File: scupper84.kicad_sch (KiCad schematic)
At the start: 172 parts, among them K1 PG1350, K10 PG1350, K11 PG1350, K12 PG1350, K13 PG1350, K14 PG1350, K15 PG1350, K16 PG1350, K17 PG1350, K18 PG1350, K19 PG1350, K2 PG1350, K20 PG1350, K21 PG1350, K22 PG1350, K23 PG1350, K24 PG1350, K25 PG1350, K26 PG1350, K27 PG1350, K28 PG1350, K29 PG1350, K3 PG1350, K30 PG1350, K31 PG1350, K32 PG1350, K33 PG1350, K34 PG1350, K35 PG1350, K36 PG1350, K37 PG1350, K38 PG1350, K39 PG1350, K4 PG1350, K40 PG1350, K41 PG1350, K42 PG1350, K43 PG1350, K44 PG1350, K45 PG1350, K46 PG1350, K47 PG1350, K48 PG1350, K49 PG1350, K5 PG1350, K50 PG1350, K51 PG1350, K52 PG1350, K53 PG1350, K54 PG1350, K55 PG1350, K56 PG1350, K57 PG1350, K58 PG1350, K59 PG1350, K6 PG1350, K60 PG1350, K61 PG1350, K62 PG1350, K63 PG1350, K64 PG1350, K65 PG1350, K66 PG1350, K67 PG1350, K68 PG1350, K69 PG1350, K7 PG1350, K70 PG1350, K71 PG1350, K72 PG1350, K73 PG1350, K74 PG1350, K75 PG1350, K76 PG1350, K77 PG1350, K78 PG1350, K79 PG1350, K8 PG1350, K80 PG1350, K81 PG1350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

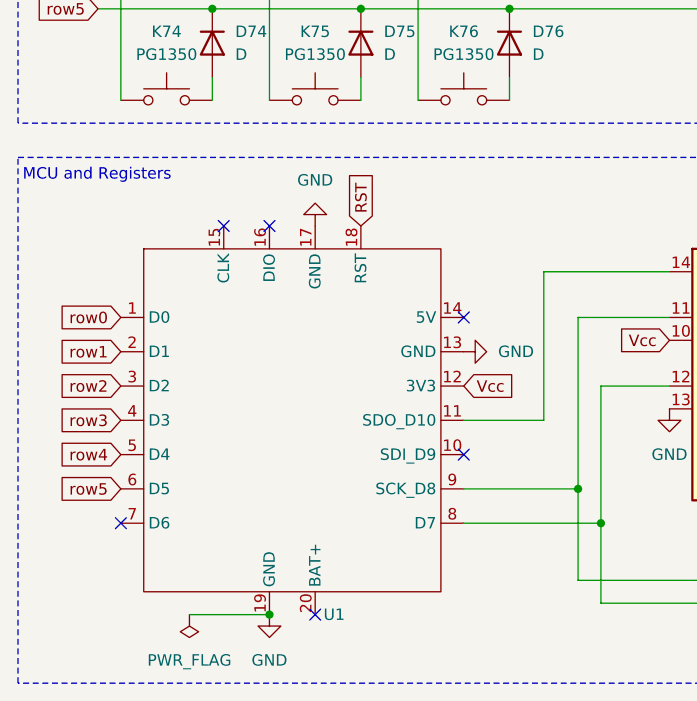
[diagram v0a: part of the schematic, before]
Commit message: Footprint for XIAO RP2040
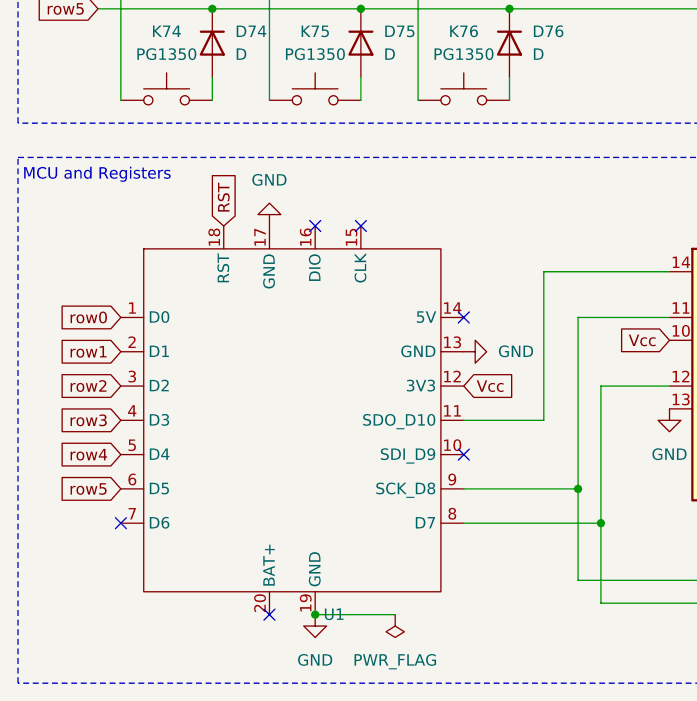
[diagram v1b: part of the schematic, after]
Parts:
- U1: footprint (none) -> keyboard_parts:XIAO RP2040 Castellated

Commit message: Drop rat's nest on PCB.
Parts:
- D1, D10, D11, D12, D13, D14, D15, D16, D17, D18, D19, D2, D20, D21, D22, D23, D24, D25, D26, D27, D28, D29, D3, D30, D31, D32, D33, D34, D35, D36, D37, D38, D39, D4, D40, D41, D42, D43, D44, D45, D46, D47, D48, D49, D5, D50, D51, D52, D53, D54, D55, D56, D57, D58, D59, D6, D60, D61, D62, D63, D64, D65, D66, D67, D68, D69, D7, D70, D71, D72, D73, D74, D75, D76, D77, D78, D79, D8, D80, D81, D82, D83, D84, D9: footprint (none) -> Diode_SMD:D_SOD-123
- K1, K10, K11, K12, K13, K14, K15, K16, K17, K18, K19, K2, K20, K21, K22, K23, K24, K25, K26, K27, K28, K29, K3, K30, K31, K32, K33, K34, K35, K36, K37, K38, K39, K4, K40, K41, K42, K43, K44, K45, K46, K47, K48, K49, K5, K50, K51, K52, K53, K54, K55, K56, K57, K58, K59, K6, K60, K61, K62, K63, K64, K65, K66, K67, K68, K69, K7, K70, K71, K72, K73, K74, K75, K76, K77, K78, K79, K8, K80, K81, K82, K83, K84, K9: footprint (none) -> Switch_Keyboard_Kailh:SW_Kailh_Choc_V1
- SW1: footprint (none) -> Button_Switch_SMD:SW_SPST_B3U-1000P
- U2, U3: footprint (none) -> Package_SO:SOIC-16_3.9x9.9mm_P1.27mm

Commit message: Work in progress on Kailh footprints.
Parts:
- K1, K10, K11, K12, K13, K14, K15, K16, K17, K18, K19, K2, K20, K21, K22, K23, K24, K25, K26, K27, K28, K29, K3, K30, K31, K32, K33, K34, K35, K36, K37, K38, K39, K4, K40, K41, K42, K43, K44, K45, K46, K47, K48, K49, K5, K50, K51, K52, K53, K54, K55, K56, K57, K58, K59, K6, K60, K61, K62, K63, K64, K65, K66, K67, K68, K69, K7, K70, K71, K72, K73, K74, K75, K76, K77, K78, K79, K8, K80, K81, K82, K83, K84, K9: footprint Switch_Keyboard_Kailh:SW_Kailh_Choc_V1 -> keyswitches:Kailh_socket_PG1350

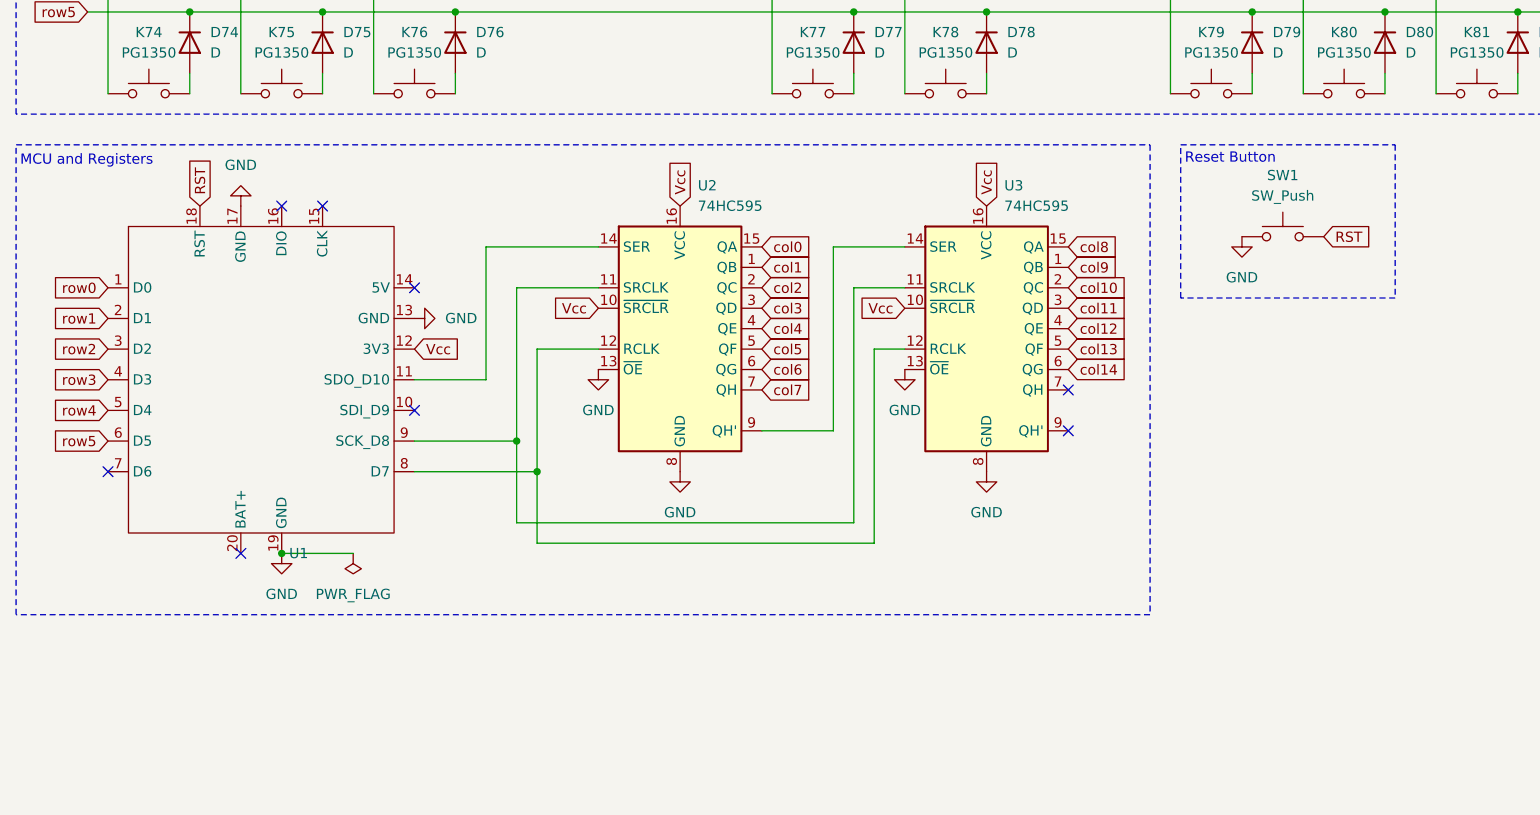
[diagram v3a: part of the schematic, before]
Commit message: Changing footprints to use my new Kailh socket footprint.
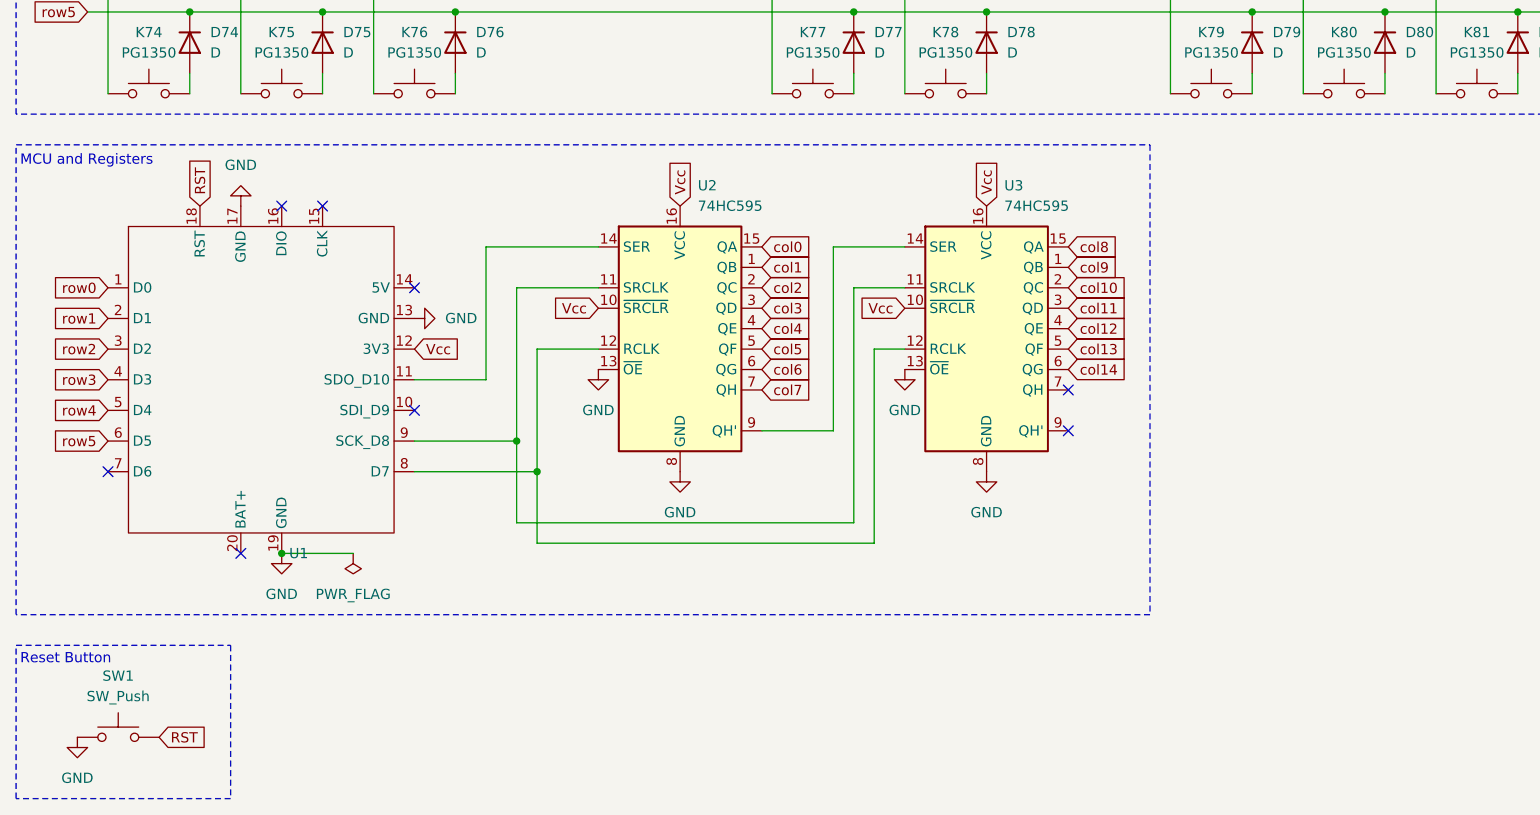
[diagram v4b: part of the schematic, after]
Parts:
- K1, K10, K11, K12, K13, K14, K15, K16, K17, K18, K19, K2, K20, K21, K22, K23, K24, K25, K26, K27, K28, K29, K3, K30, K31, K32, K33, K34, K35, K36, K37, K38, K39, K4, K40, K41, K42, K43, K44, K45, K46, K47, K48, K49, K5, K50, K51, K52, K53, K54, K55, K56, K57, K58, K59, K6, K60, K61, K62, K63, K64, K65, K66, K67, K68, K69, K7, K70, K71, K72, K73, K74, K75, K76, K77, K78, K79, K8, K80, K81, K82, K83, K84, K9: footprint keyswitches:Kailh_socket_PG1350 -> keyboard_parts:Socket_PG1350_Hotswap
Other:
- moved on the sheet: SW1

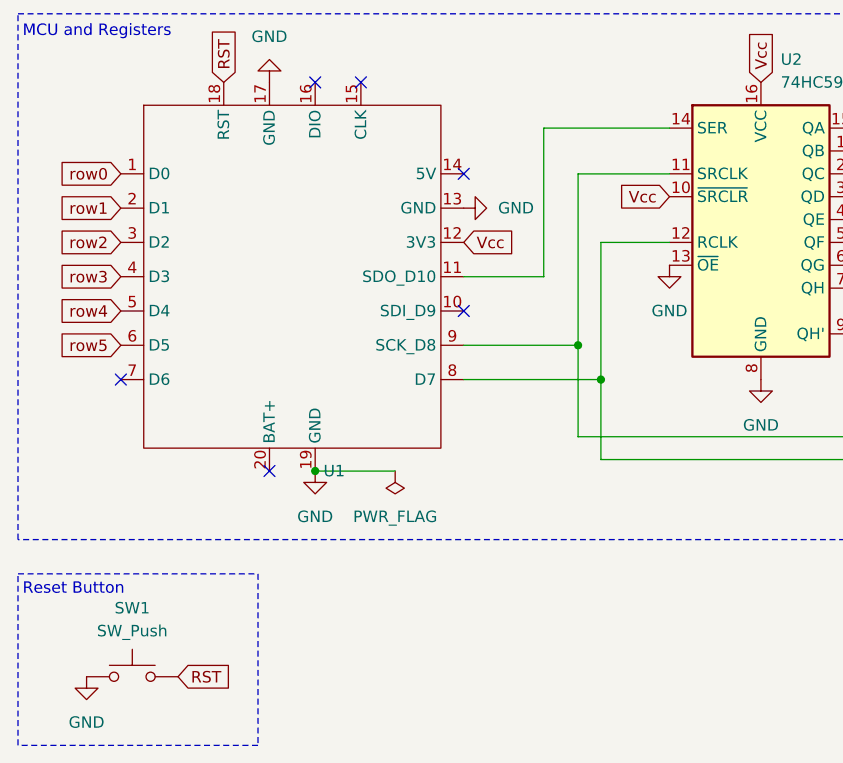
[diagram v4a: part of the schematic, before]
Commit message: Arranging keys in their staggered array. Keys bigger than 1u may still need some adjustment.
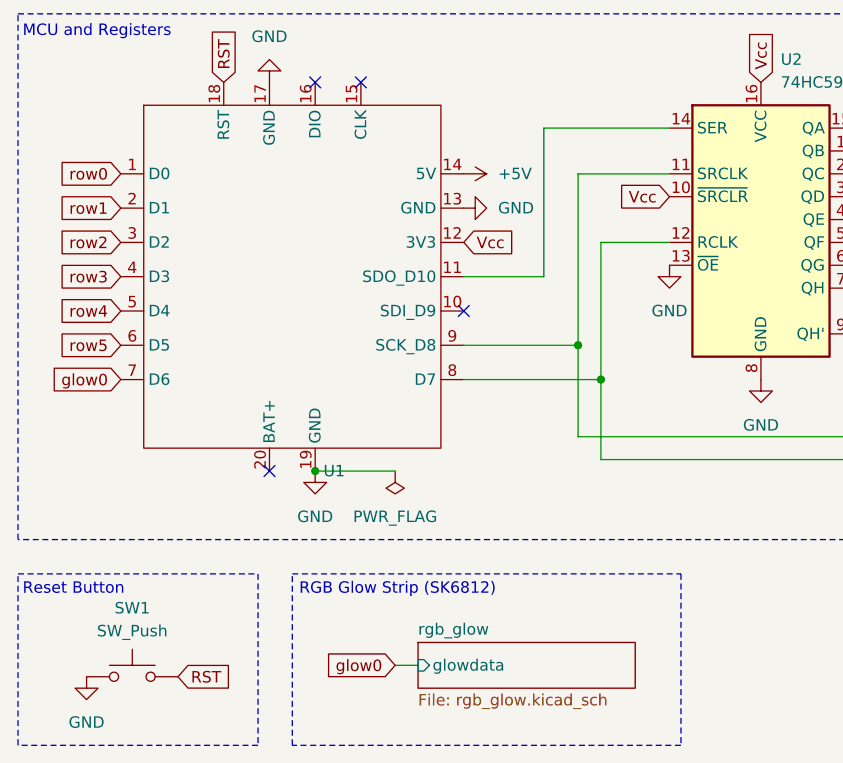
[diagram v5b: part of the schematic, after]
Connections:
- net +5V: now reaches U1.14 (5V)
- net glow0: now reaches U1.7 (D6)
- no-connect marks 8 -> 6
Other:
- added sheet rgb_glow (rgb_glow.kicad_sch)
- note added: "RGB Glow Strip (SK6812)"
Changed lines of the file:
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@@
 	)
 	(no_connect
-		(at 30.48 148.59)
-	)
-	(no_connect
 		(at 52.07 115.57)
 	)
@@
 	)
 	(no_connect
-		(at 68.58 125.73)
-	)
-	(no_connect
 		(at 46.99 158.75)
 	)
@@
 	(wire
 		(pts
+			(xy 60.96 180.34) (xy 63.5 180.34)
+		)
+		(stroke
+			(width 0)
+			(type default)
+		)
+	)
+	(wire
+		(pts
 			(xy 245.11 50.8) (xy 245.11 63.5)
 		)
@@
 	)
 	(rectangle
+		(start 49.53 170.18)
+		(end 92.71 189.23)
+		(stroke
+			(width 0)
+			(type dash)
+		)
+		(fill
+			(type none)
+		)
+	)
+	(rectangle
 		(start 19.05 16.51)
 		(end 279.4 104.14)
@@
 		)
 	)
+	(text "RGB Glow Strip (SK6812)"
+		(exclude_from_sim no)
+		(at 50.292 171.196 0)
+		(effects
+			(font
+				(size 1.27 1.27)
+			)
+			(justify left top)
+		)
+	)
 	(text "Reset Button"
 		(exclude_from_sim no)
@@
 		)
 	)
+	(global_label "glow0"
+		(shape input)
+		(at 30.48 148.59 180)
+		(fields_autoplaced yes)
+		(effects
+			(font
+				(size 1.27 1.27)
+			)
+			(justify right)
+		)
+		(property "Intersheetrefs" "${INTERSHEET_REFS}"
+			(at 23.2011 148.59 0)
+			(effects
+				(font
+					(size 1.27 1.27)
+				)
+				(justify right)
+				(hide yes)
+			)
+		)
+	)
 	(global_label "col0"
 		(shape input)
@@
 		)
 	)
+	(global_label "glow0"
+		(shape input)
+		(at 60.96 180.34 180)
+		(fields_autoplaced yes)
+		(effects
+			(font
+				(size 1.27 1.27)
+			)
+			(justify right)
+		)
+		(property "Intersheetrefs" "${INTERSHEET_REFS}"
+			(at 52.4716 180.34 0)
+			(effects
+				(font
+					(size 1.27 1.27)
+				)
+				(justify right)
+				(hide yes)
+			)
+		)
+	)
 	(global_label "row3"
 		(shape input)
@@
 	)
 	(symbol
+		(lib_id "power:+5V")
+		(at 68.58 125.73 270)
+		(unit 1)
+		(exclude_from_sim no)
+		(in_bom yes)
+		(on_board yes)
+		(dnp no)
+		(fields_autoplaced yes)
+		(property "Reference" "#PWR09"
+			(at 64.77 125.73 0)
+			(effects
+				(font
+					(size 1.27 1.27)
+				)
+				(hide yes)
+			)
+		)
+		(property "Value" "+5V"
+			(at 72.39 125.7299 90)
+			(effects
+				(font
+					(size 1.27 1.27)
+				)
+				(justify left)
+			)
+		)
+		(property "Footprint" ""
+			(at 68.58 125.73 0)
+			(effects
+				(font
+					(size 1.27 1.27)
+				)
+				(hide yes)
+			)
+		)
+		(property "Datasheet" ""
+			(at 68.58 125.73 0)
+			(effects
+				(font
+					(size 1.27 1.27)
+				)
+				(hide yes)
+			)
+		)
+		(property "Description" "Power symbol creates a global label with name \"+5V\""
+			(at 68.58 125.73 0)
+			(effects
+				(font
+					(size 1.27 1.27)
+				)
+				(hide yes)
+			)
+		)
+		(pin "1"
+		)
+		(instances
+			(project ""
+				(path "/779ef5c1-cac4-4837-8440-65dc0477817c"
+					(reference "#PWR09")
+					(unit 1)
+				)
+			)
+		)
+	)
+	(symbol
 		(lib_id "keyboard_parts:PG1350")
 		(at 134.62 101.6 0)
@@
 				)
 			)
+		)
+	)
+	(sheet
+		(at 63.5 177.8)
+		(size 24.13 5.08)
+		(fields_autoplaced yes)
+		(stroke
+			(width 0.1524)
+			(type solid)
+		)
+		(fill
+			(color 0 0 0 0.0000)
+		)
+		(property "Sheetname" "rgb_glow"
+			(at 63.5 177.0884 0)
+			(effects
+				(font
+					(size 1.27 1.27)
+				)
+				(justify left bottom)
+			)
+		)
+		(property "Sheetfile" "rgb_glow.kicad_sch"
+			(at 63.5 183.4646 0)
+			(effects
+				(font
+					(size 1.27 1.27)
+				)
+				(justify left top)
+			)
+		)
+		(pin "glowdata" input
+			(at 63.5 180.34 180)
+			(effects
+				(font
+					(size 1.27 1.27)
+				)
+				(justify left)
+			)
+		)
+		(instances
+			(project "scupper84"
+				(path "/779ef5c1-cac4-4837-8440-65dc0477817c"
+					(page "2")
+				)
+			)
